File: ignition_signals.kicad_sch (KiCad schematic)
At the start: 10 parts, among them U11 EL3H7, U9 EL3H7

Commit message: Uploaded image for ReadME
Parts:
- renumbered U11 to U6, U9 to U6
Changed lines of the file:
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@@
   (symbol (lib_id "Isolator:EL817") (at 136.525 107.95 0) (unit 1)
     (in_bom yes) (on_board yes) (dnp no) (fields_autoplaced)
-    (property "Reference" "U11" (at 136.525 99.06 0)
+    (property "Reference" "U6" (at 136.525 99.06 0)
       (effects (font (size 1.27 1.27)))
     )
@@
     (instances
       (project "Controls-LeaderDaughterPCB"
-        (path "/c7871779-04fe-4705-8150-20a4dd0ef44f/0d7b9330-5178-458e-b803-9c8d464fd559"
-          (reference "U11") (unit 1)
-        )
         (path "/c7871779-04fe-4705-8150-20a4dd0ef44f/f7827f80-0f50-4e4f-b2cd-ff48878538ae"
           (reference "U6") (unit 1)
@@
         (path "/c7871779-04fe-4705-8150-20a4dd0ef44f/fd5723b9-3644-4daa-af29-4c44667f673c"
           (reference "U7") (unit 1)
+        )
+        (path "/c7871779-04fe-4705-8150-20a4dd0ef44f/0d7b9330-5178-458e-b803-9c8d464fd559"
+          (reference "U11") (unit 1)
         )
       )
@@
   (symbol (lib_id "Isolator:EL817") (at 136.525 75.565 0) (unit 1)
     (in_bom yes) (on_board yes) (dnp no) (fields_autoplaced)
-    (property "Reference" "U9" (at 136.525 66.675 0)
+    (property "Reference" "U6" (at 136.525 66.675 0)
       (effects (font (size 1.27 1.27)))
     )
@@
     (instances
       (project "Controls-LeaderDaughterPCB"
-        (path "/c7871779-04fe-4705-8150-20a4dd0ef44f/0d7b9330-5178-458e-b803-9c8d464fd559"
-          (reference "U9") (unit 1)
-        )
         (path "/c7871779-04fe-4705-8150-20a4dd0ef44f/f7827f80-0f50-4e4f-b2cd-ff48878538ae"
           (reference "U6") (unit 1)
@@
           (reference "U7") (unit 1)
         )
+        (path "/c7871779-04fe-4705-8150-20a4dd0ef44f/0d7b9330-5178-458e-b803-9c8d464fd559"
+          (reference "U9") (unit 1)
+        )
       )

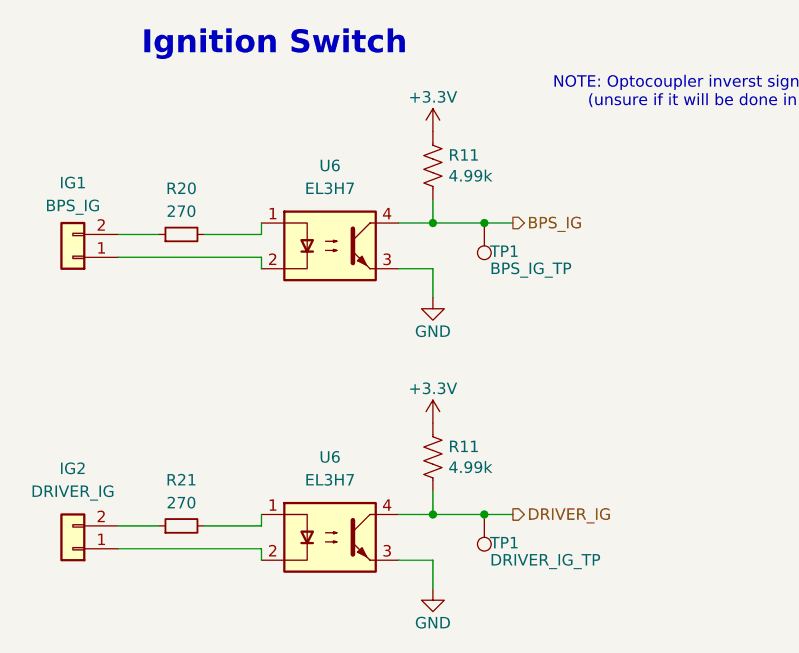
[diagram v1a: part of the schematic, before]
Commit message: Switch ignition switch signal's resistor from pull-up to pull-down
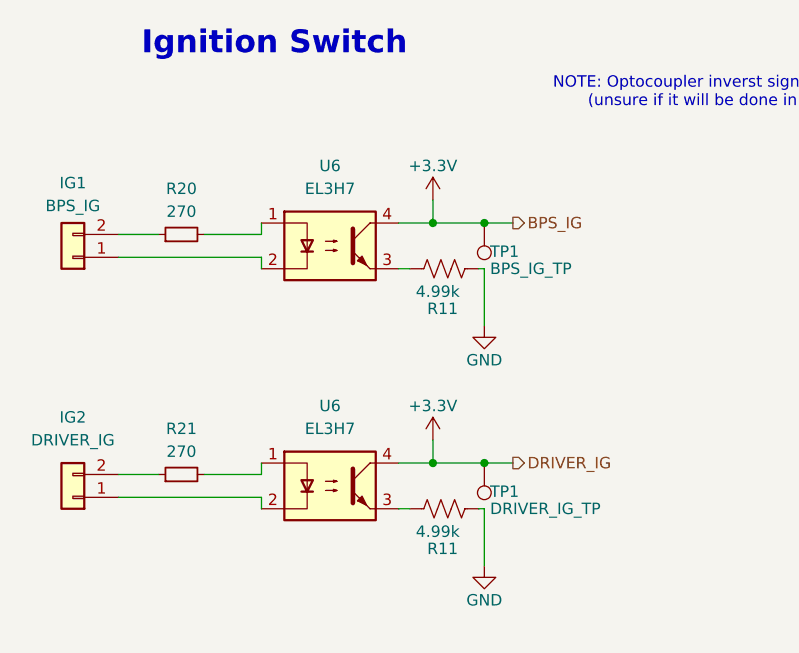
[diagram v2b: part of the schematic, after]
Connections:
- net +3.3V: now also TP1.1, TP1.1, U6.4, U6.4; no longer R11.1, R11.1
- net GND: now also R11.1, R11.1; no longer U6.3, U6.3
- removed net BPS_IG: R11.2, TP1.1, U6.4
- removed net DRIVER_IG: R11.2, TP1.1, U6.4
- new net: R11.2, U6.3 (x2)
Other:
- moved on the sheet: IG2, R11, R21, TP1, U6

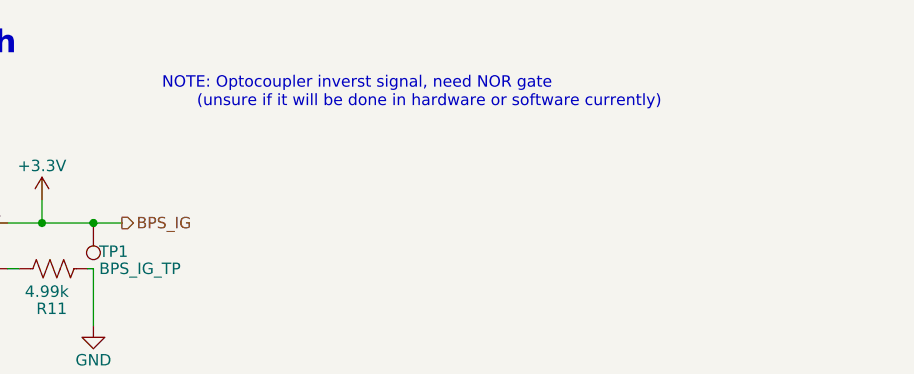
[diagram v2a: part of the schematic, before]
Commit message: Fixed leaderSOM connections, removed optocouplers for lighting and fans, found new MOSFETs
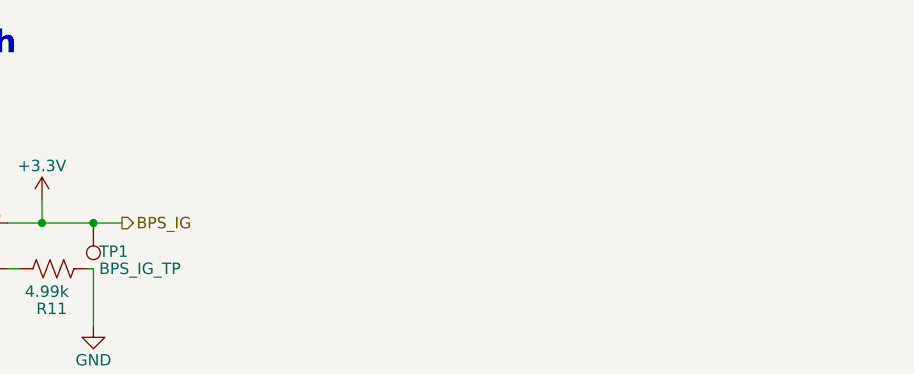
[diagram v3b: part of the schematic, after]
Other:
- note removed: "NOTE: Optocoupler inverst signal, need NOR gate (unsure if it will be done in hardware or software currently)"
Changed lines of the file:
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@@
     (effects (font (size 2.54 2.54) (thickness 0.508) bold) (justify left bottom))
-  )
-  (text "NOTE: Optocoupler inverst signal, need NOR gate \n       (unsure if it will be done in hardware or software currently)"
-    (at 161.29 60.325 0)
-    (effects (font (size 1.27 1.27)) (justify left bottom))
   )
   (hierarchical_label "DRIVER_IG" (shape output) (at 156.845 99.695 0) (fields_autoplaced)

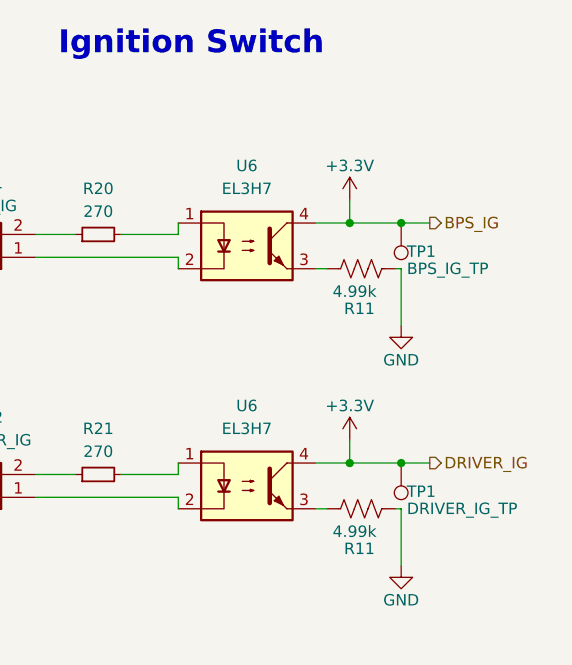
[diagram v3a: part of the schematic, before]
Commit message: Added I2C GPIO expander to reduce GPIO pins from LeaderSOM and replace 555 timer circuit. Adjusted ignition switch signals.
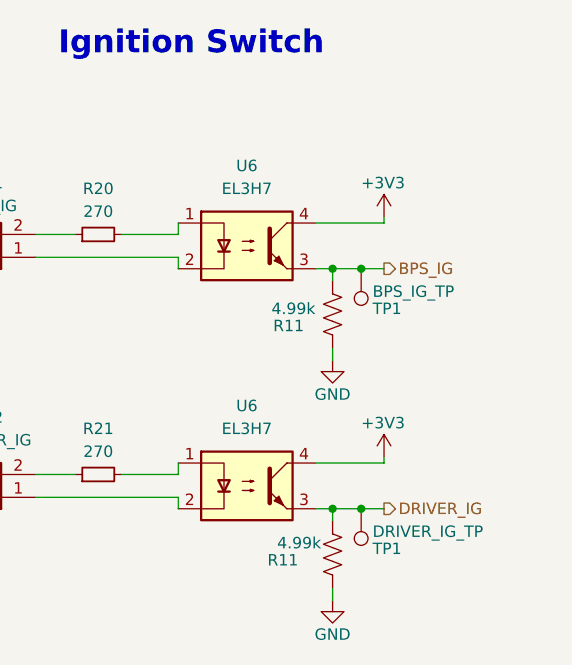
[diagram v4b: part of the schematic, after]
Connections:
- net DRIVER_IG: now reaches R11.2, U6.3
- net DRIVER_IG: now also TP1.1
- net BPS_IG: now reaches R11.2, U6.3
- net BPS_IG: now also TP1.1
- net +3.3V renamed +3V3
- net +3V3: no longer TP1.1, TP1.1
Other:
- moved on the sheet: R11, TP1

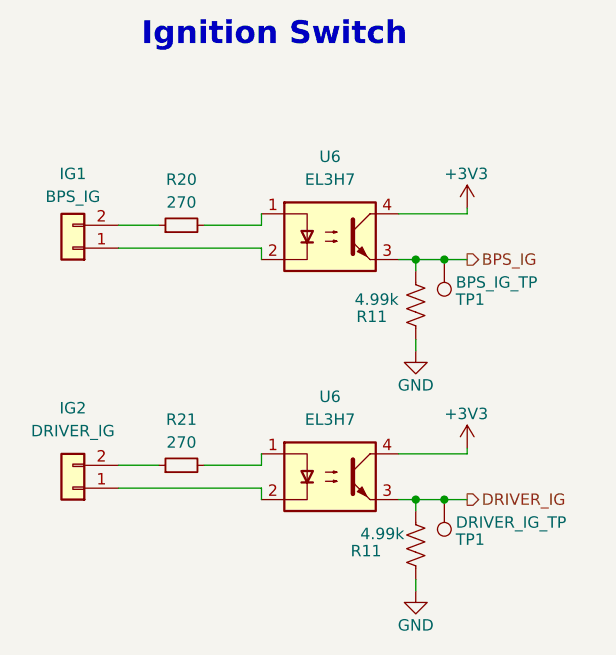
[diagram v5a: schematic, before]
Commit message: organized schematic, changed resistor values, moved ignition signals to IC
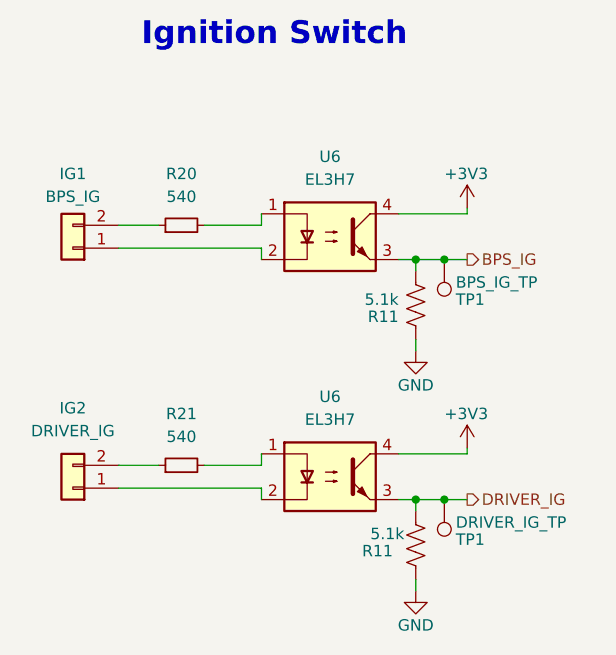
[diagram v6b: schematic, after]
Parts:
- R11: value 4.99k -> 5.1k
- R20, R21: value 270 -> 540
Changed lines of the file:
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@@
   (symbol (lib_id "Device:R_Small") (at 120.015 100.965 90) (unit 1)
     (in_bom yes) (on_board yes) (dnp no) (fields_autoplaced)
-    (property "Reference" "R21" (at 120.015 95.885 90)
-      (effects (font (size 1.27 1.27)))
-    )
-    (property "Value" "270" (at 120.015 98.425 90)
+    (property "Reference" "R21" (at 120.015 95.25 90)
+      (effects (font (size 1.27 1.27)))
+    )
+    (property "Value" "540" (at 120.015 97.79 90)
       (effects (font (size 1.27 1.27)))
     )
@@
   (symbol (lib_id "Device:R_US") (at 146.05 83.185 180) (unit 1)
     (in_bom yes) (on_board yes) (dnp no)
-    (property "Reference" "R11" (at 142.875 84.455 0)
-      (effects (font (size 1.27 1.27)) (justify left))
-    )
-    (property "Value" "4.99k" (at 144.145 82.55 0)
+    (property "Reference" "R11" (at 144.145 84.455 0)
+      (effects (font (size 1.27 1.27)) (justify left))
+    )
+    (property "Value" "5.1k" (at 144.145 82.55 0)
       (effects (font (size 1.27 1.27)) (justify left))
     )
@@
   (symbol (lib_id "Device:R_US") (at 146.05 109.855 180) (unit 1)
     (in_bom yes) (on_board yes) (dnp no)
-    (property "Reference" "R11" (at 142.24 110.49 0)
-      (effects (font (size 1.27 1.27)) (justify left))
-    )
-    (property "Value" "4.99k" (at 144.78 108.585 0)
+    (property "Reference" "R11" (at 143.51 110.49 0)
+      (effects (font (size 1.27 1.27)) (justify left))
+    )
+    (property "Value" "5.1k" (at 144.78 108.585 0)
       (effects (font (size 1.27 1.27)) (justify left))
     )
@@
   (symbol (lib_id "Device:R_Small") (at 120.015 74.295 90) (unit 1)
     (in_bom yes) (on_board yes) (dnp no) (fields_autoplaced)
-    (property "Reference" "R20" (at 120.015 69.215 90)
-      (effects (font (size 1.27 1.27)))
-    )
-    (property "Value" "270" (at 120.015 71.755 90)
-      (effects (font (size 1.27 1.27)))
-    )
+    (property "Reference" "R20" (at 120.015 68.58 90)
+      (effects (font (size 1.27 1.27)))
+    )
+    (property "Value" "540" (at 120.015 71.12 90)
+      (effects (font (size 1.27 1.27)))
+    )

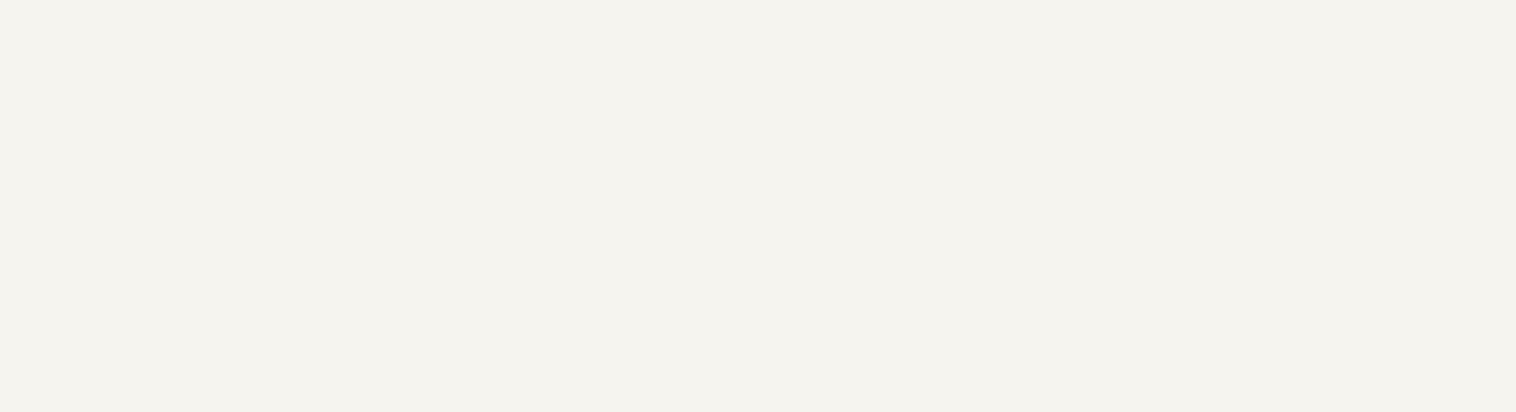
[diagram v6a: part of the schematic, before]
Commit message: added notes section to bottom of sheets
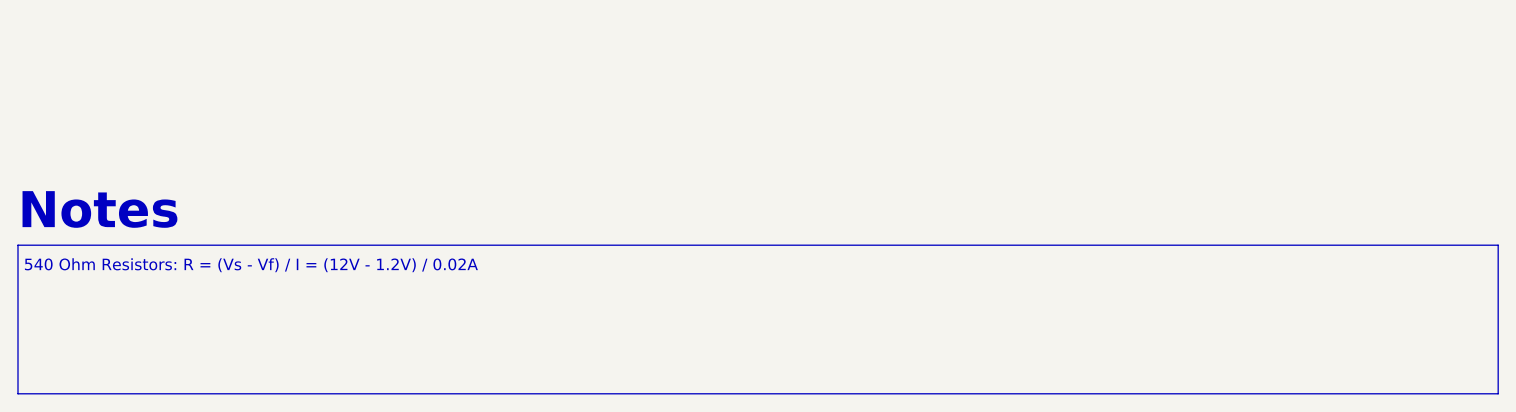
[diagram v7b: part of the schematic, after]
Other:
- note added: "540 Ohm Resistors: R = (Vs - Vf) / I = (12V - 1.2V) / 0.02A"
- note added: "Notes"
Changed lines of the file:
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@@
     (stroke (width 0) (type default))
+  )
+  (rectangle (start 12.065 181.61) (end 176.53 198.12)
+    (stroke (width 0) (type default))
+    (fill (type none))
+  )
+  (text "540 Ohm Resistors: R = (Vs - Vf) / I = (12V - 1.2V) / 0.02A"
+    (at 12.7 184.785 0)
+    (effects (font (size 1.27 1.27)) (justify left bottom))
   )
   (text "Ignition Switch" (at 115.57 54.61 0)
     (effects (font (size 2.54 2.54) (thickness 0.508) bold) (justify left bottom))
   )
+  (text "Notes" (at 12.065 180.34 0)
+    (effects (font (size 4 4) (thickness 0.8) bold) (justify left bottom))
+  )
   (hierarchical_label "DRIVER_IG" (shape output) (at 151.765 104.775 0) (fields_autoplaced)

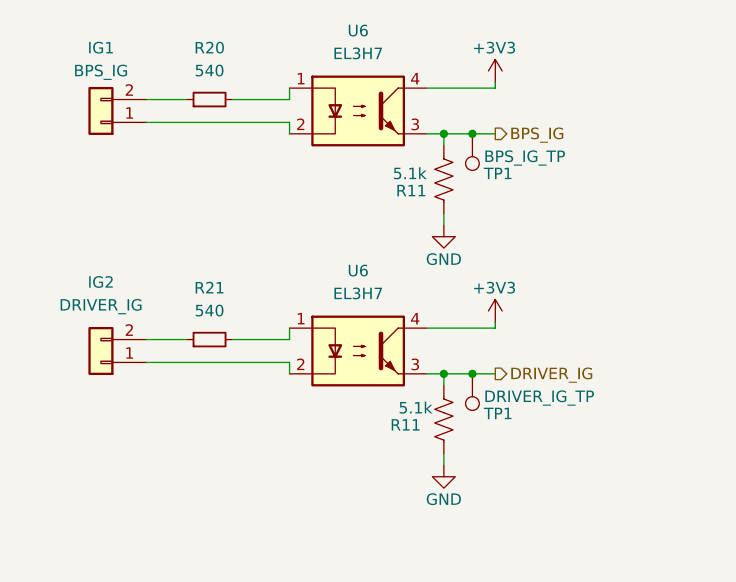
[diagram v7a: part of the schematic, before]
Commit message: Added to notes and changed resistor values
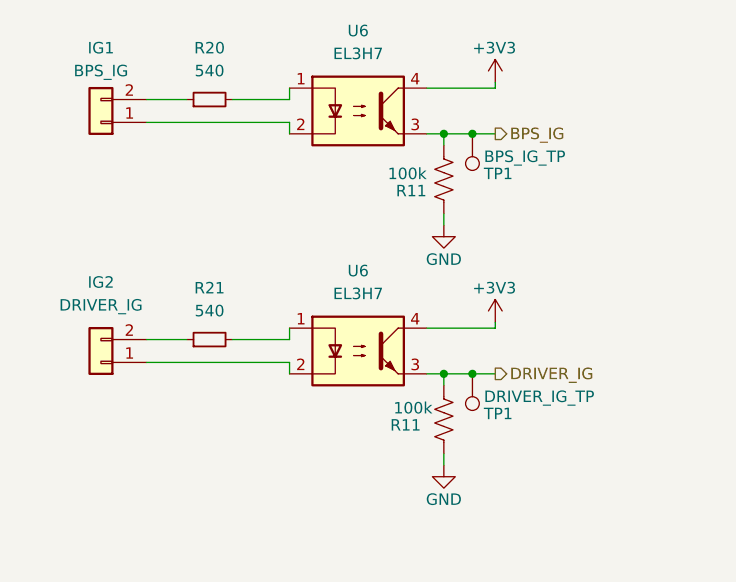
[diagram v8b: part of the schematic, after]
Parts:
- R11: value 5.1k -> 100k
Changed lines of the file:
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@@
       (effects (font (size 1.27 1.27)) (justify left))
     )
-    (property "Value" "5.1k" (at 144.145 82.55 0)
+    (property "Value" "100k" (at 144.145 82.55 0)
       (effects (font (size 1.27 1.27)) (justify left))
     )
@@
       (effects (font (size 1.27 1.27)) (justify left))
     )
-    (property "Value" "5.1k" (at 144.78 108.585 0)
+    (property "Value" "100k" (at 144.78 108.585 0)
       (effects (font (size 1.27 1.27)) (justify left))
     )
